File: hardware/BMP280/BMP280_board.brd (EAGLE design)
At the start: 17.6 x 17.6 mm, 8 parts, among them U1 BMP280, U2 EM406FLAT

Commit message: BMP280
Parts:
- removed C3, C4, C5, C6: 56pF, SparkFun-Capacitors:0603-CAP
- added R1: (no value), SparkFun-Passives:0603-RES
- C1: value 0.1uF -> 1.0uF
- moved U1 2.25 mm to (8.62, 11.6)
- moved U2 1.41 mm to (7.62, 2.34)
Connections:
- new net N$1: R1.2, U1.5
- net CSB: no longer C3.1
- net GND: no longer C3.2, C4.2, C5.2, C6.2
- net SCK: no longer C5.1
- net SDI: no longer C4.1
- net SDO: now also R1.1; no longer C6.1, U1.5
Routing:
- net CSB: track 21.7 -> 9.02 mm
- net SDI: track 18.5 -> 8.12 mm
- net GND: track 13.8 -> 7.69 mm, vias 9 -> 5
- net SCK: track 10.7 -> 7.22 mm
- net VCC: track 16.8 -> 13.8 mm
- net SDO: track 7.38 -> 4.76 mm
- net N$1: track 0.00 -> 2.00 mm
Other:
- board size 17.6 x 17.6 mm -> 14.6 x 14.6 mm

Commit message: MS5803
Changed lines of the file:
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@@
 <contactref element="C1" pad="2"/>
 <contactref element="C2" pad="2"/>
-<via x="2.032" y="9.398" extent="1-16" drill="0.5" diameter="0.254"/>
-<via x="2.032" y="7.112" extent="1-16" drill="0.5" diameter="0.254"/>
-<wire x1="2.032" y1="9.398" x2="3.595" y2="9.398" width="0.254" layer="1"/>
-<wire x1="2.032" y1="7.112" x2="3.595" y2="7.112" width="0.254" layer="1"/>
-<wire x1="3.595" y1="7.112" x2="3.595" y2="7.239" width="0.254" layer="1"/>
 <via x="6.35" y="11.938" extent="1-16" drill="0.6"/>
 <via x="10.668" y="12.7" extent="1-16" drill="0.6"/>
@@
 <wire x1="6.39" y1="11.898" x2="7.82" y2="11.898" width="0.254" layer="1"/>
 <wire x1="9.42" y1="12.548" x2="10.516" y2="12.548" width="0.254" layer="1"/>
-<wire x1="3.595" y1="9.398" x2="3.595" y2="9.525" width="0" layer="19" extent="1-1"/>
+<via x="2.032" y="9.652" extent="1-16" drill="0.6"/>
+<via x="2.032" y="7.366" extent="1-16" drill="0.6"/>
+<wire x1="3.595" y1="7.239" x2="3.595" y2="9.525" width="0" layer="19" extent="1-1"/>
+<wire x1="3.595" y1="9.525" x2="2.159" y2="9.525" width="0.4064" layer="1"/>
+<wire x1="2.159" y1="9.525" x2="2.032" y2="9.652" width="0.4064" layer="1"/>
+<wire x1="3.595" y1="7.239" x2="2.159" y2="7.239" width="0.4064" layer="1"/>
+<wire x1="2.159" y1="7.239" x2="2.032" y2="7.366" width="0.4064" layer="1"/>
 </signal>
 <signal name="CSB">

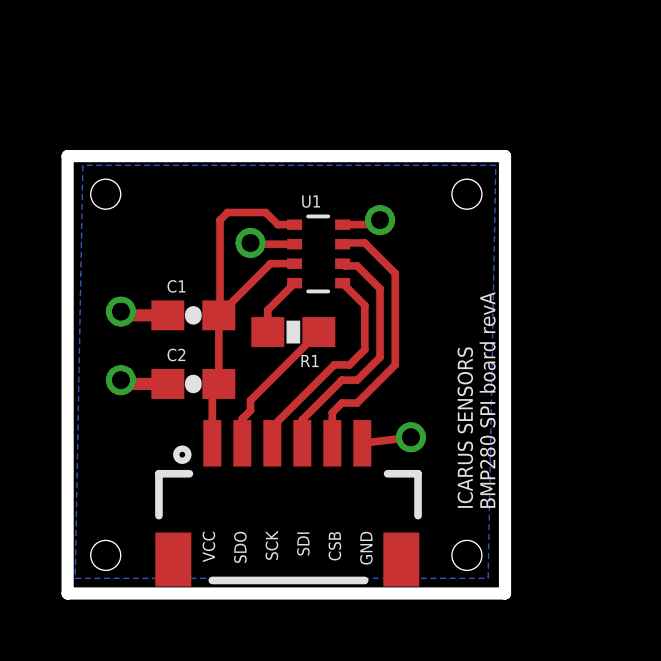
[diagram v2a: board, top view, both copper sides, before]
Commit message: borderless
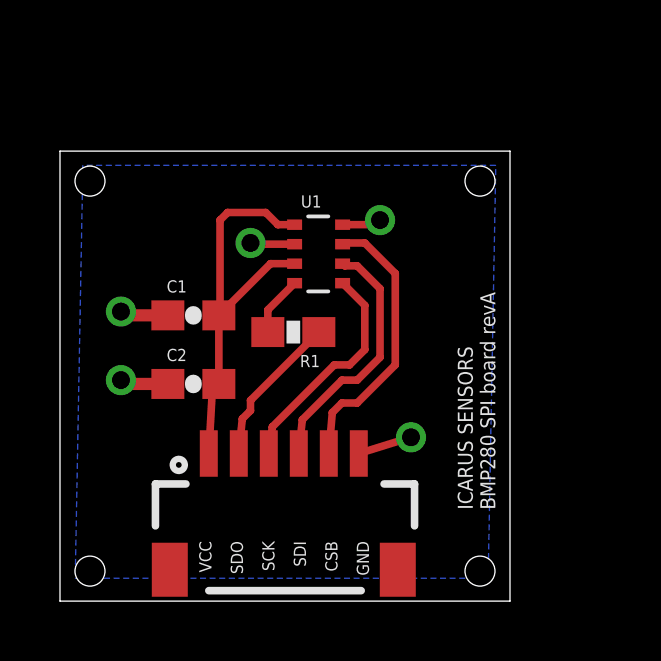
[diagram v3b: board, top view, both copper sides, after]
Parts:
- moved U2 0.36 mm to (7.50, 2.00)
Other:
- board size 14.6 x 14.6 mm -> 15 x 15 mm
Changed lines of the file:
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@@
 <board>
 <plain>
-<wire x1="0.254" y1="0.254" x2="0.254" y2="14.834" width="0.4064" layer="20"/>
-<wire x1="0.254" y1="14.834" x2="14.834" y2="14.834" width="0.4064" layer="20"/>
-<wire x1="14.834" y1="14.834" x2="14.834" y2="0.254" width="0.4064" layer="20"/>
-<wire x1="14.834" y1="0.254" x2="0.254" y2="0.254" width="0.4064" layer="20"/>
-<hole x="1.524" y="13.564" drill="1"/>
-<hole x="13.564" y="13.564" drill="1"/>
-<hole x="13.564" y="1.524" drill="1"/>
-<hole x="1.524" y="1.524" drill="1"/>
+<wire x1="0" y1="0" x2="0" y2="15" width="0" layer="20"/>
+<wire x1="0" y1="15" x2="15" y2="15" width="0" layer="20"/>
+<wire x1="15" y1="15" x2="15" y2="0" width="0" layer="20"/>
+<wire x1="15" y1="0" x2="0" y2="0" width="0" layer="20"/>
+<hole x="1" y="14" drill="1"/>
+<hole x="14" y="14" drill="1"/>
+<hole x="14" y="1" drill="1"/>
+<hole x="1" y="1" drill="1"/>
 <text x="14.51" y="3.048" size="0.5" layer="25" rot="R90">ICARUS SENSORS
 BMP280 SPI board revA</text>
@@
 <attribute name="NAME" x="8.029" y="13.119" size="0.4064" layer="25" rot="R180" align="top-right"/>
 </element>
-<element name="U2" library="icarus_sensors" package="EM406-FLAT" value="EM406FLAT" x="7.617" y="2.34" smashed="yes"/>
+<element name="U2" library="icarus_sensors" package="EM406-FLAT" value="EM406FLAT" x="7.5" y="2" smashed="yes"/>
 <element name="R1" library="SparkFun-Passives" package="0603-RES" value="" x="7.778" y="8.968" rot="R180"/>
 </elements>
@@
 <vertex x="14.526" y="14.526"/>
 </polygon>
-<wire x1="10.077" y1="5.26" x2="11.7" y2="5.461" width="0.254" layer="1"/>
+<wire x1="9.96" y1="4.92" x2="11.7" y2="5.461" width="0.254" layer="1"/>
 <via x="11.7" y="5.461" extent="1-16" drill="0.6"/>
 <contactref element="C1" pad="2"/>
@@
 <contactref element="U1" pad="2"/>
 <contactref element="U2" pad="5"/>
-<wire x1="9.077" y1="5.26" x2="9.077" y2="6.283" width="0.254" layer="1"/>
+<wire x1="8.96" y1="4.92" x2="9.077" y2="6.283" width="0.254" layer="1"/>
 <wire x1="9.077" y1="6.283" x2="9.398" y2="6.604" width="0.254" layer="1"/>
 <wire x1="9.398" y1="6.604" x2="9.906" y2="6.604" width="0.254" layer="1"/>
@@
 <contactref element="U1" pad="4"/>
 <contactref element="U2" pad="3"/>
-<wire x1="7.077" y1="5.26" x2="7.077" y2="5.807" width="0.254" layer="1"/>
+<wire x1="6.96" y1="4.92" x2="7.077" y2="5.807" width="0.254" layer="1"/>
 <wire x1="7.077" y1="5.807" x2="9.144" y2="7.874" width="0.254" layer="1"/>
 <wire x1="9.144" y1="7.874" x2="9.652" y2="7.874" width="0.254" layer="1"/>
@@
 <contactref element="U2" pad="2"/>
 <contactref element="R1" pad="1"/>
-<wire x1="6.077" y1="5.26" x2="6.077" y2="6.077" width="0.254" layer="1"/>
+<wire x1="5.96" y1="4.92" x2="6.077" y2="6.077" width="0.254" layer="1"/>
 <wire x1="6.077" y1="6.077" x2="6.35" y2="6.35" width="0.254" layer="1"/>
 <wire x1="6.35" y1="6.35" x2="6.35" y2="6.69" width="0.254" layer="1"/>
@@
 <contactref element="U1" pad="3"/>
 <contactref element="U2" pad="4"/>
-<wire x1="8.077" y1="5.26" x2="8.077" y2="6.045" width="0.254" layer="1"/>
+<wire x1="7.96" y1="4.92" x2="8.077" y2="6.045" width="0.254" layer="1"/>
 <wire x1="8.077" y1="6.045" x2="9.398" y2="7.366" width="0.254" layer="1"/>
 <wire x1="9.398" y1="7.366" x2="9.906" y2="7.366" width="0.254" layer="1"/>
@@
 <wire x1="5.295" y1="7.239" x2="5.295" y2="9.525" width="0.254" layer="1"/>
 <wire x1="5.08" y1="9.564" x2="5.295" y2="9.525" width="0.254" layer="1"/>
-<wire x1="5.077" y1="5.26" x2="5.077" y2="7.021" width="0.254" layer="1"/>
+<wire x1="4.96" y1="4.92" x2="5.077" y2="7.021" width="0.254" layer="1"/>
 <wire x1="5.077" y1="7.021" x2="5.295" y2="7.239" width="0.254" layer="1"/>
 <wire x1="7.82" y1="12.548" x2="7.264" y2="12.548" width="0.254" layer="1"/>
